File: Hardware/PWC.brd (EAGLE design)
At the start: 78 x 47 mm, 45 parts, among them IC1 DS3502, IC2 DS3502, IC3 ESPWROOM32, IC5 CP2102N-A01-GQFN24, J1 OUTPUT, J2 USB-C-16P-16P, J3 BUT5, Q1 MMDT3904

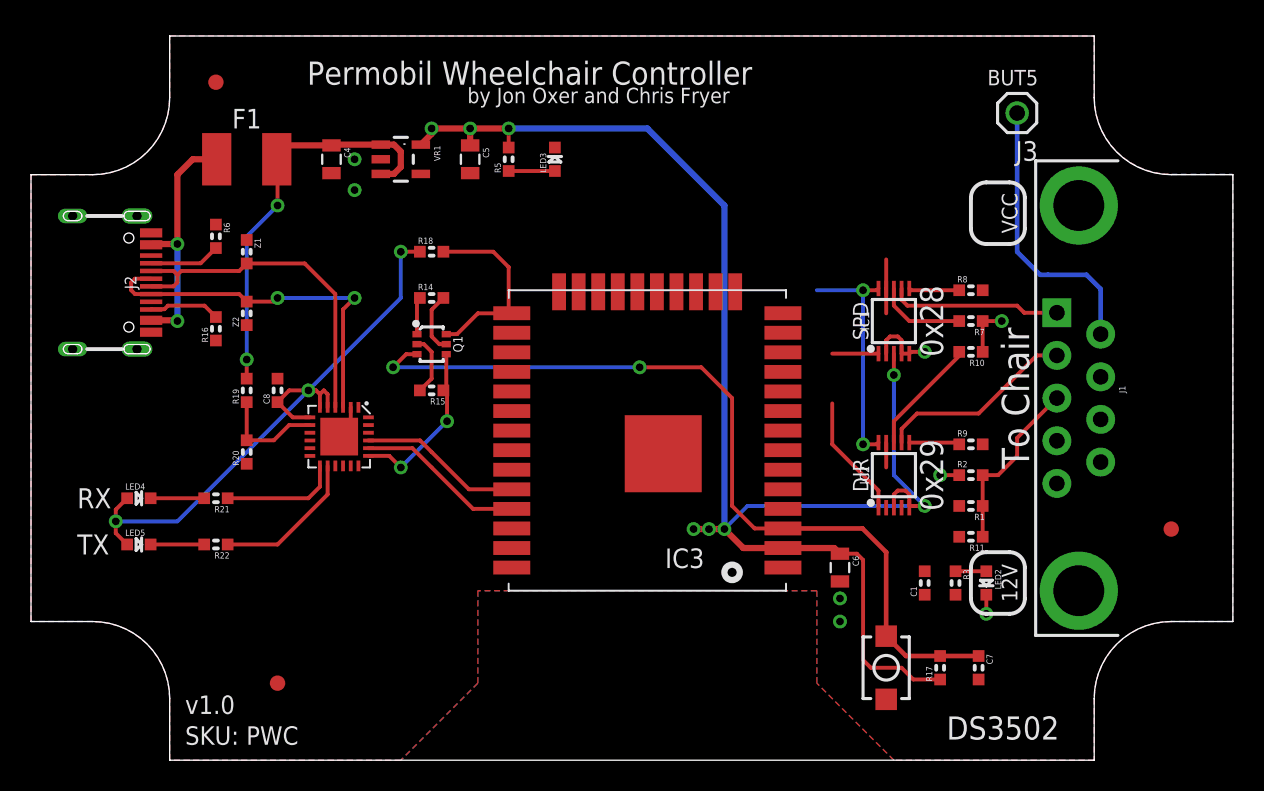
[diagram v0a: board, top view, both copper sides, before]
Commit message: Routing, silkscreen, designators, ERC / DRC for v1.0 release.
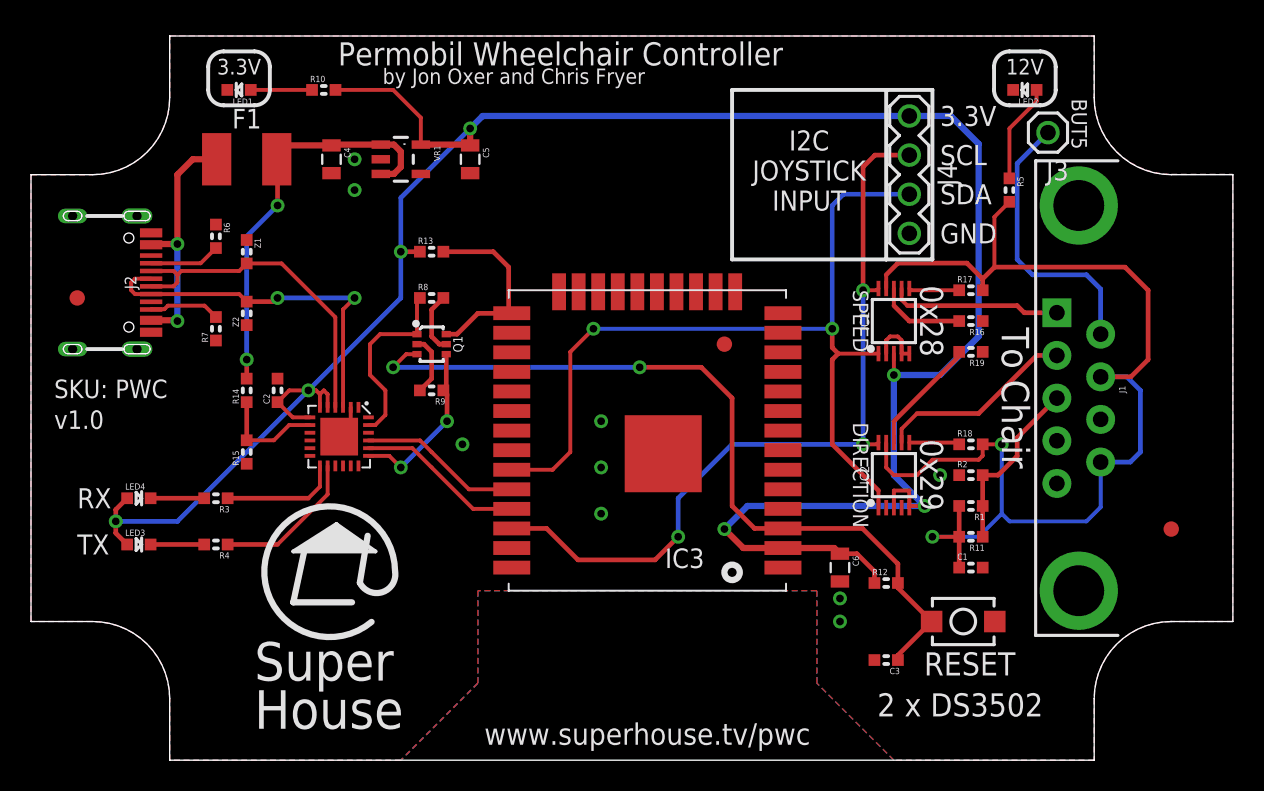
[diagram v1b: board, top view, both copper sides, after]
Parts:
- removed C7: 1uF, SuperHouse-DiscreteSemi:C0603
- removed LED5: TX/YEL, SuperHouse-LEDs:LED-0603
- removed R20: 47.5K, SuperHouse-DiscreteSemi:R0603
- removed R21: 1K, SuperHouse-DiscreteSemi:R0603
- removed S2: RESET, SuperHouse-Switches:TACTILE_SMT_3X4X2
- added C3: 1uF, SuperHouse-DiscreteSemi:C0603
- added J4: JOYSTICK, SuperHouse-Connectors:1X04
- added LED1: BLUE, SuperHouse-LEDs:LED-0603
- added R12, R13: 22.1K, SuperHouse-DiscreteSemi:R0603
- added S1: RESET, SuperHouse-Switches:TACTILE_SMT_3X4X2
- LED3: value BLUE -> TX/YEL
- R10, R8, R9: value 0R -> 10K
- R11: value 22K -> 22.1K
- R14: value 10K -> 22.1K
- R15: value 10K -> 47.5K
- R16: value 5.1K -> 0R
- R17, R18: value 22K -> 0R
- R19: value 22.1K -> 0R
- R3: value 4K7 -> 1K
- R5: value 10K -> 4K7
- R7: value 0R -> 5.1K
- moved R16 49.0 mm to (61.0, 28.5), turned to 180 degrees
- moved R7 49.0 mm to (12.0, 28.0), turned to 90 degrees
- moved R3 48.3 mm to (12.0, 17.0), turned to 180 degrees
- moved R19 47.1 mm to (61.0, 26.5), turned to 180 degrees
- moved R10 45.3 mm to (19.0, 43.5), turned to 0 degrees
- moved R18 37.2 mm to (61.0, 20.5)
- moved LED3 36.8 mm to (7.00, 14.0), turned to 0 degrees
- moved U$36 36.4 mm to (45.0, 27.0)
- moved R9 35.2 mm to (26.0, 24.0), turned to 180 degrees
- moved R8 35.0 mm to (26.0, 30.0)
- moved R5 32.6 mm to (63.5, 37.0), turned to 270 degrees
- moved LED2 32.1 mm to (64.5, 43.5), turned to 180 degrees
- moved R17 24.6 mm to (61.0, 30.5), turned to 0 degrees
- moved U$35 16.6 mm to (3.00, 30.0)
- moved R14 13.4 mm to (14.0, 24.0), turned to 90 degrees
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- renumbered C8 to C2, IC5 to IC4, R22 to R4
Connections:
- net !RESET: now also C3.1, R12.2, S1.2; no longer C7.1, R17.2, S2.2
- net 12V: now also R17.2, R18.2, R5.2; no longer R3.2, R8.2, R9.2
- net 3.3V: now also J4.1, LED3.A, R10.2, R12.1, R13.1; no longer LED5.A, R17.1, R18.1, R5.2
- net 5V: now also R14.2; no longer R19.2
- net DTR: now also R8.1; no longer R14.1
- net GND: now also C3.2, J4.4, LED1.C, R15.1, R19.1, S1.1; no longer C7.2, LED3.C, R10.1, R20.1, S2.1
- net GPIO0: now also R13.2; no longer R18.2
- net N$1: now also LED1.A, R10.1; no longer LED3.A, R5.1
- net N$10: now also R7.2; no longer R16.2
- net N$13: now also LED3.C; no longer LED5.C
- net N$15: now also R19.2; no longer R10.2
- net N$2: now also R17.1; no longer R8.1
- net N$3: now also R18.1; no longer R9.1
- net N$39: now also R14.1, R15.2; no longer R19.1, R20.2
- net N$4: now also R16.2; no longer R7.2
- net N$6: now also R5.1; no longer R3.1
- net N$7: now also R8.2; no longer R14.2
- net N$8: now also R9.2; no longer R15.2
- net N$9: now also R3.2; no longer R21.2
- net RTS: now also R9.1; no longer R15.1
- net RX_LED: now also R3.1; no longer R21.1
- net SCL: now also J4.2
- net SDA: now also J4.3
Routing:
- net 12V: track 5.11 -> 78.7 mm, vias 0 -> 2
- net SDA: track 11.0 -> 57.5 mm, vias 0 -> 2
- net SCL: track 15.1 -> 51.6 mm, vias 2 -> 3
- net 3.3V: track 138.2 -> 156.0 mm, vias 11 -> 7
- net DTR: track 2.43 -> 12.1 mm
- net GND: track 12.4 -> 5.64 mm, vias 6 -> 9
- net N$6: track 2.00 -> 6.47 mm
- net !RESET: track 55.0 -> 52.1 mm
- net N$1: track 3.00 -> 3.98 mm
- net D-: track 22.8 -> 22.0 mm
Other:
- board text added: "2 x DS3502"
- board text added: "3.3V"
- board text added: "A"
- board text added: "DIRECTION"
- board text added: "GND"
- board text added: "I2C JOYSTICK INPUT"
- board text added: "K"
- board text added: "RESET"
- board text added: "SCL"
- board text added: "SDA"
- board text added: "SPEED"
- board text removed: "DIR"
- board text removed: "DS3502"
- board text removed: "SPD"
- board text removed: "VCC"
